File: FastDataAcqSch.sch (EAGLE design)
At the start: 205 parts, among them IC1 LT1963AEQ, IC2 FT230XQ, IC3 ADCMP553BRMZ, J1 USB_MICROAB_SMT, J2 MICRO-FIT_3.0_2POS_RA_SMD, X1 SMA-142-0701-801/806, X2 87832-14, X3 SMA-142-0701-801/806, Y1 SI530-500, Y2 DNP, Y3 100MHz

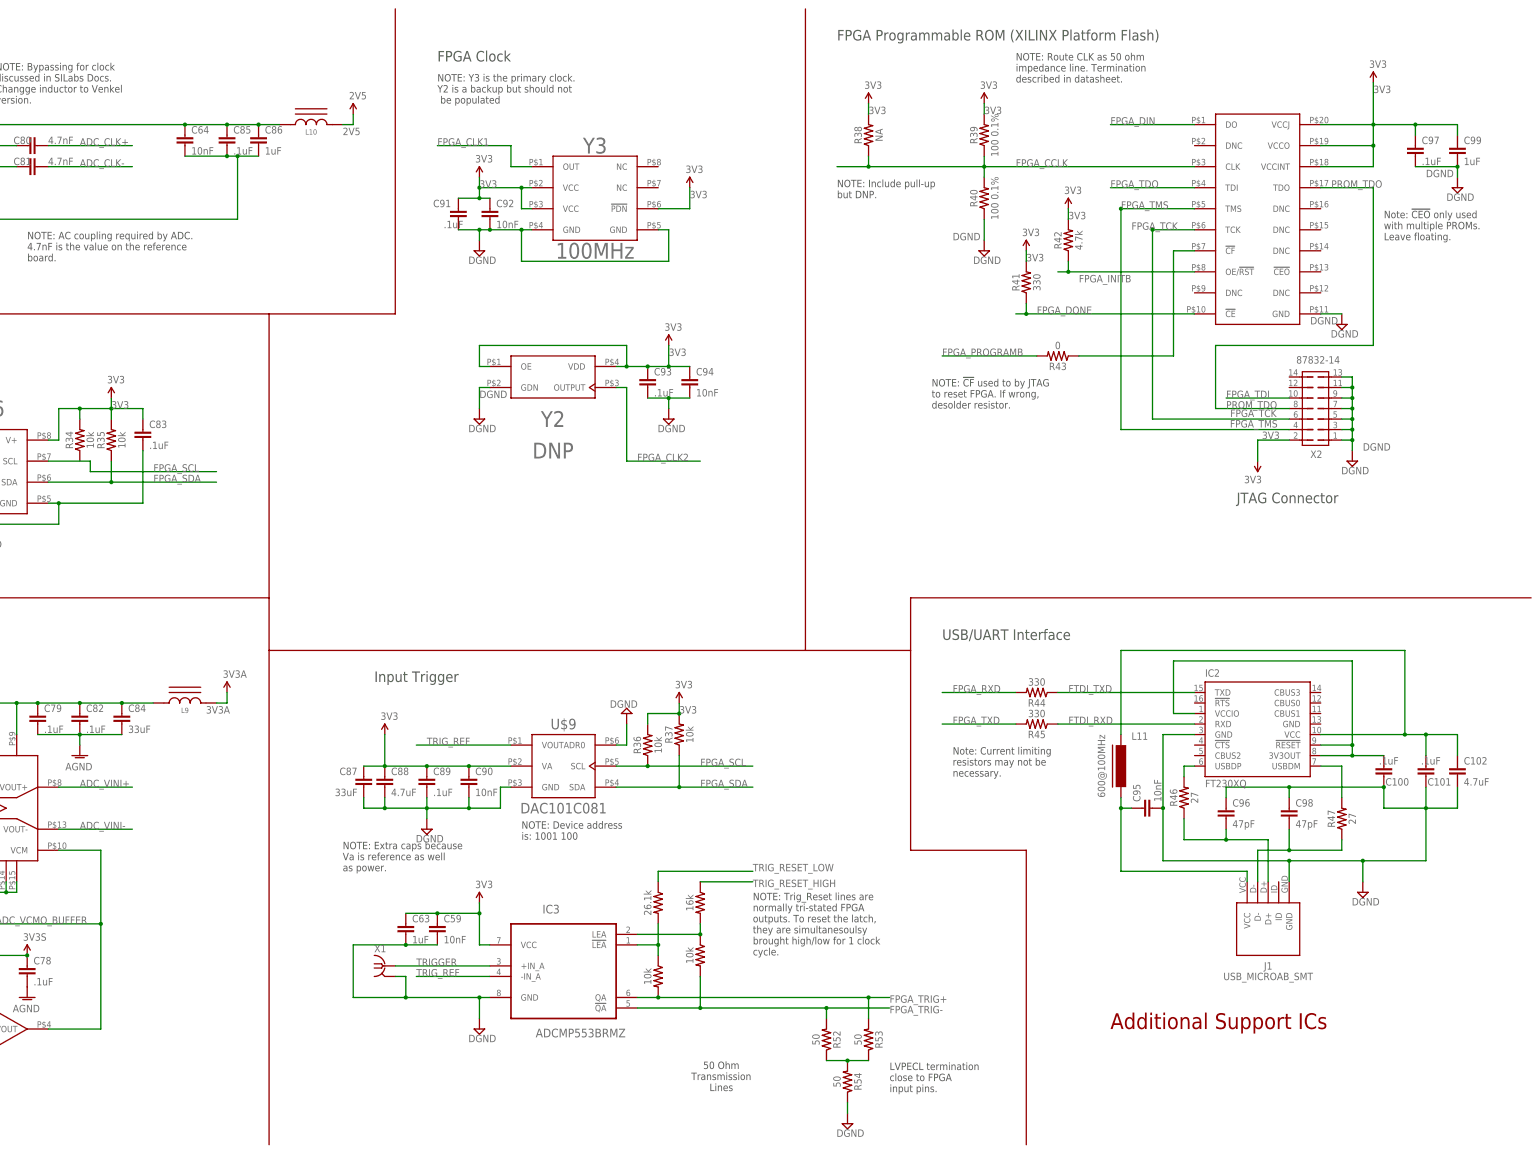
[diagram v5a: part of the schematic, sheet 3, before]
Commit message: Unchecked Finalized Schematic
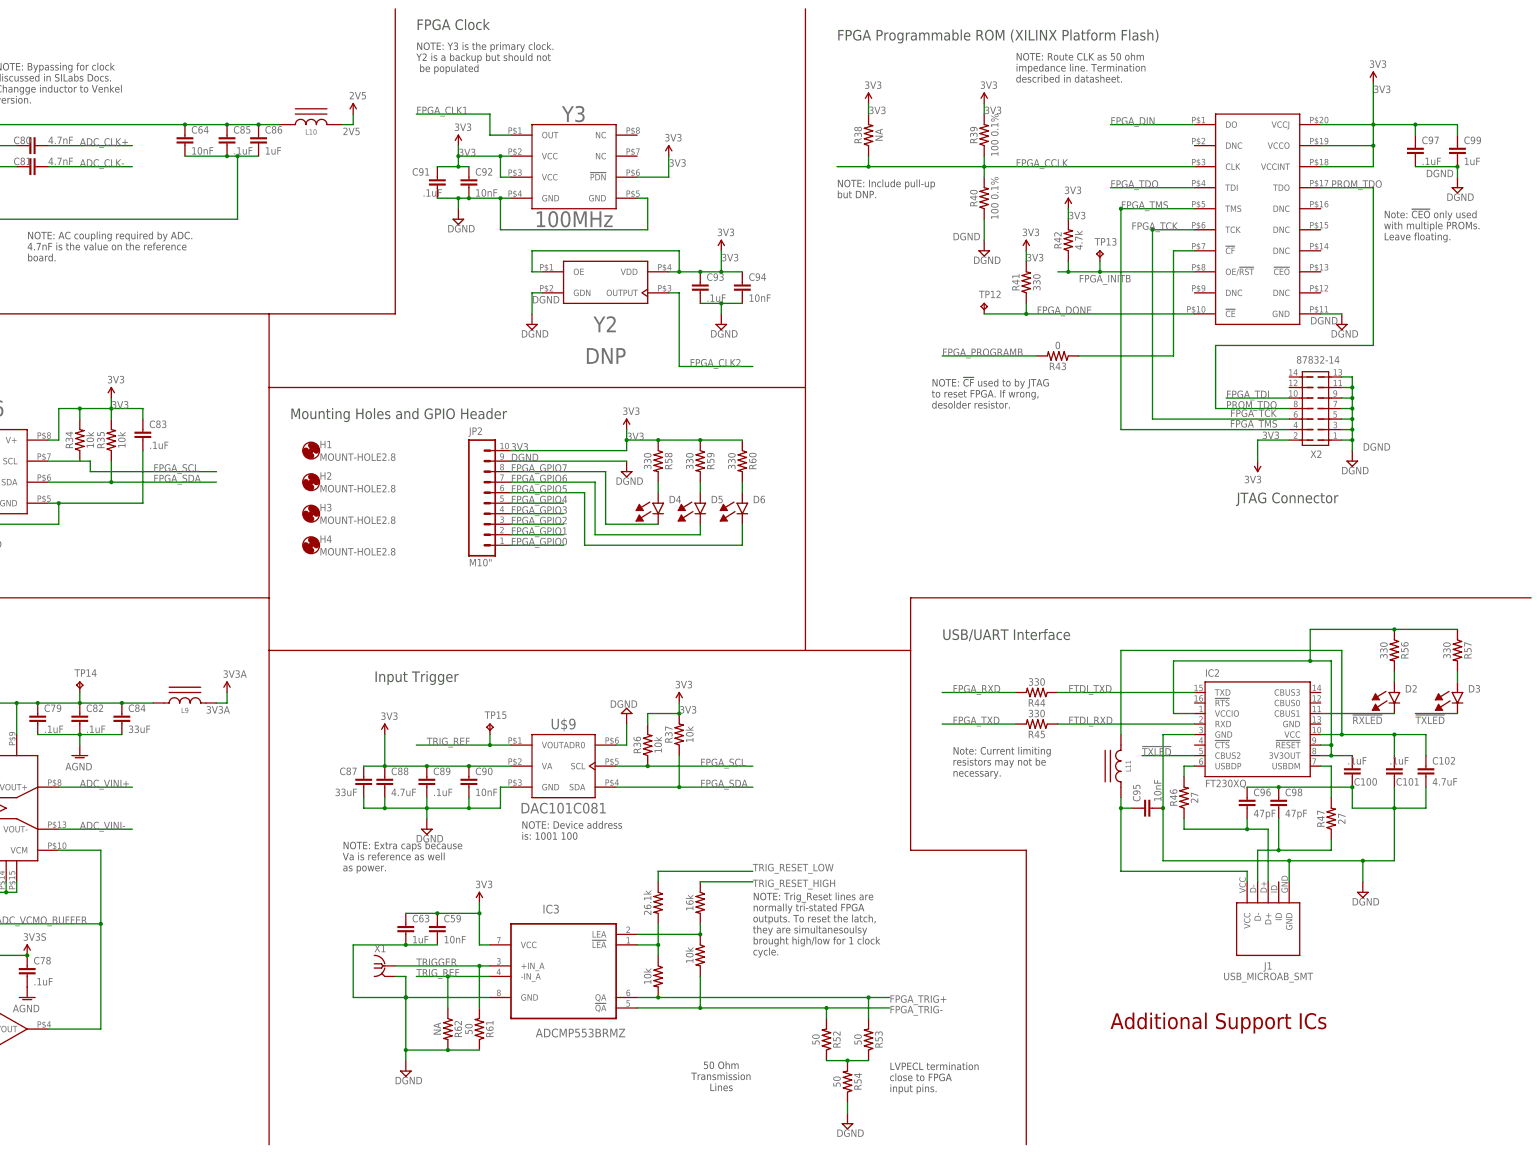
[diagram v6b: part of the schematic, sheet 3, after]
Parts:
- removed C16: NA, rcl:C-EUC0603
- added D1, D6: (no value), Schuyler:LED_0603_RED
- added D2, D5: (no value), Schuyler:LED_0603_GREEN
- added D3, D4: (no value), Schuyler:LED_0603_BLUE
- added H1, H2, H3, H4: MOUNT-HOLE2.8, holes:MOUNT-HOLE2.8
- added JP2: M10", SparkFun-Connectors:M10"
- added JP3: (no value), SparkFun-Passives:JUMPER-2PTH
- added R56, R57, R58, R59, R60: 330, rcl:R-US_R0201
- added R61: 50, rcl:R-US_R0201
- added R62: NA, rcl:R-US_R0603
- added TP10, TP11, TP12, TP13, TP14, TP15: TPPAD1-13, testpad:TPPAD1-13
- L11: value 600@100MHz -> (none); device dp_devices:FERRITE-0603 -> Schuyler:FERRITE_BEADS_BLM18SG331; PARTNUMBER 240-2371-1-ND -> (none); SUPPLIER DIGIKEY -> (none)
- R23: value 806K -> 10k; MANPARTNUMBER (none) -> RC0603J103CS; MANUFACTURER (none) -> Samsung Electro-Mechanics America, Inc; PARTNUMBER P806KABCT-ND -> 1276-3817-1-ND
- R24: value 150K -> 1k; PARTNUMBER 1276-3719-1-ND -> 1276-3797-1-ND
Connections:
- new net !RXLED: D2.CATHODE, IC2.CBUS1
- new net !TXLED: D3.CATHODE, IC2.CBUS2
- new net FPGA_GPIO0: JP2.1, U$2.IO_L49P_D3_2
- new net FPGA_GPIO1: JP2.2, U$2.IO_L14N_D12_2
- new net FPGA_GPIO2: JP2.3, U$2.IO_L14P_D11_2
- new net FPGA_GPIO3: JP2.4, U$2.IO_L13N_D10_2
- new net FPGA_GPIO4: JP2.5, U$2.IO_L12N_D2_MISO3_2
- new net FPGA_GPIO5: D6.CATHODE, JP2.6, U$2.IO_L12P_D1_MISO2_2
- new net FPGA_GPIO6: D5.CATHODE, JP2.7, U$2.IO_L3N_MOSI_CSI_B_MISO0_2
- new net FPGA_GPIO7: D4.CATHODE, JP2.8, U$2.IO_L2P_CMPCLK_2
- new net N$10: D2.ANODE, R56.2
- new net N$19: D6.ANODE, R60.2
- new net N$21: D5.ANODE, R59.2
- new net N$22: D4.ANODE, R58.2
- new net N$26: U$2.GND@10, U$2.GND@8, U$2.GND@9
- new net N$9: D1.ANODE, R24.1
- net 1V2: now also U$2.VCCINT@4
- net 1V8: now also U$2.GND@7
- net 3V3: now also JP2.10, R58.1, R59.1, R60.1, U$2.VCCAUX@4; no longer R23.2
- net 3V3S: now also TP14.TP
- net 5VUSB: now also L11.P$2; no longer L11.1
- net 5VUSB_CON: now also L11.P$1; no longer L11.2
- net DGND: now also D1.CATHODE, JP2.9, R61.1, R62.2; no longer C16.2, R24.2
- net FPGA_DONE: now also TP12.TP
- net FPGA_INITB: now also TP13.TP
- net N$1: now also JP3.2
- net N$13: now also D3.ANODE, R57.2; no longer C16.1, R23.1, R24.1, U$3G$4.EN
- net N$17: now also JP3.1, R24.2
- net N$8: now also R56.1, R57.1
- net PGOOD: now also R23.1, TP11.TP, U$2.IO_L49N_D4_2
- net S_TEMP: now also TP10.TP
- net TRIGGER: now also R61.2
- net TRIG_REF: now also R62.1, TP15.TP
- net VIN: now also U$3G$4.EN
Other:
- note added: "Mounting Holes and GPIO Header"
- note added: "Note: 1V8 must be enabled before FPGA starts config process so that HSWAPEN is high and all FPGA pins are tri-stated."
- note added: "Power Sequencing: 1) 1V2 and 1V8 supply are always enabled. 2) 3V3 enable once 1V2 is ready 3) ADC 1V9 enabled from FPGA 4) 2V5 and 3V3A enabled from FPGA. These shoud only be enabled after 1V9 is stable."
- note removed: "Power Sequencing: 1) 1V2 supply is always enabled. 2) 3V3 enable once 1V2 is ready 3) 1V8 enabled once 3V3 is ready 4) ADC 1V9 enabled from FPGA 5) 2V5 and 3V3A enabled from FPGA. These shoud only be enabled after 1V9 is stable."
- moved on the sheet: C100, C101, C102, C12, C26, C29, C3, C91, C92, C93, C94, C96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
